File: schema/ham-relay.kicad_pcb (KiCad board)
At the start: 2 copper layers, 62 parts, among them P1 CONN_01X08, P2 RESET, P3 ISP, P4 CONN_01X03, P5 JTAG, U1 CPC1017N, U2 XYZ, U3 REG 3V3, U4 XYZ, U5 TBB1458, U6 LPC1114FN28/102

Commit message: Update schematics
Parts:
- added TP1: TESTPOINT, Measurement_Points:Measurement_Point_Round-SMD-Pad_Small, F.Cu at (189.2, 41.9)
- added TP10: TESTPOINT, Measurement_Points:Measurement_Point_Round-SMD-Pad_Small, F.Cu at (228.6, 20.3)
- added TP2: TESTPOINT, Measurement_Points:Measurement_Point_Round-SMD-Pad_Small, F.Cu at (264.2, 113.0)
- added TP3: TESTPOINT, Measurement_Points:Measurement_Point_Round-SMD-Pad_Small, F.Cu at (251.5, 139.7)
- added TP4: TESTPOINT, Measurement_Points:Measurement_Point_Round-SMD-Pad_Small, F.Cu at (195.6, 152.4)
- added TP5: TESTPOINT, Measurement_Points:Measurement_Point_Round-SMD-Pad_Small, F.Cu at (226.1, 113.0)
- added TP6: TESTPOINT, Measurement_Points:Measurement_Point_Round-SMD-Pad_Small, F.Cu at (264.2, 73.7)
- added TP7: TESTPOINT, Measurement_Points:Measurement_Point_Round-SMD-Pad_Small, F.Cu at (195.6, 138.4)
- added TP8: TESTPOINT, Measurement_Points:Measurement_Point_Round-SMD-Pad_Small, F.Cu at (189.2, 34.3)
- added TP9: TESTPOINT, Measurement_Points:Measurement_Point_Round-SMD-Pad_Small, F.Cu at (217.2, 20.3)
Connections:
- C15 pad 2: /MOD_OUT -> /AUDIO_OUT
- P3 pad 1: GND -> Net-(P3-Pad1)
- P3 pad 2: Net-(P3-Pad2) -> GND
- R21 pad 1: /MOD_OUT -> /AUDIO_OUT
- R22 pad 2: Net-(P3-Pad2) -> Net-(P3-Pad1)
- U3 pad 1: VCC -> (no net)
- U3 pad 2: +3V3 -> (no net)
- U3 pad 3: GND -> (no net)
- U6 pad 24: Net-(P3-Pad2) -> Net-(P3-Pad1)
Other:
- board text added: "+12V"
- board text added: "+3V3"
- board text added: "AUDIO_OUT"
- board text added: "GND"
- board text added: "TONE"
- board text added: "TONE_SW"
- board text added: "VCC"
- board text added: "VCC/2"

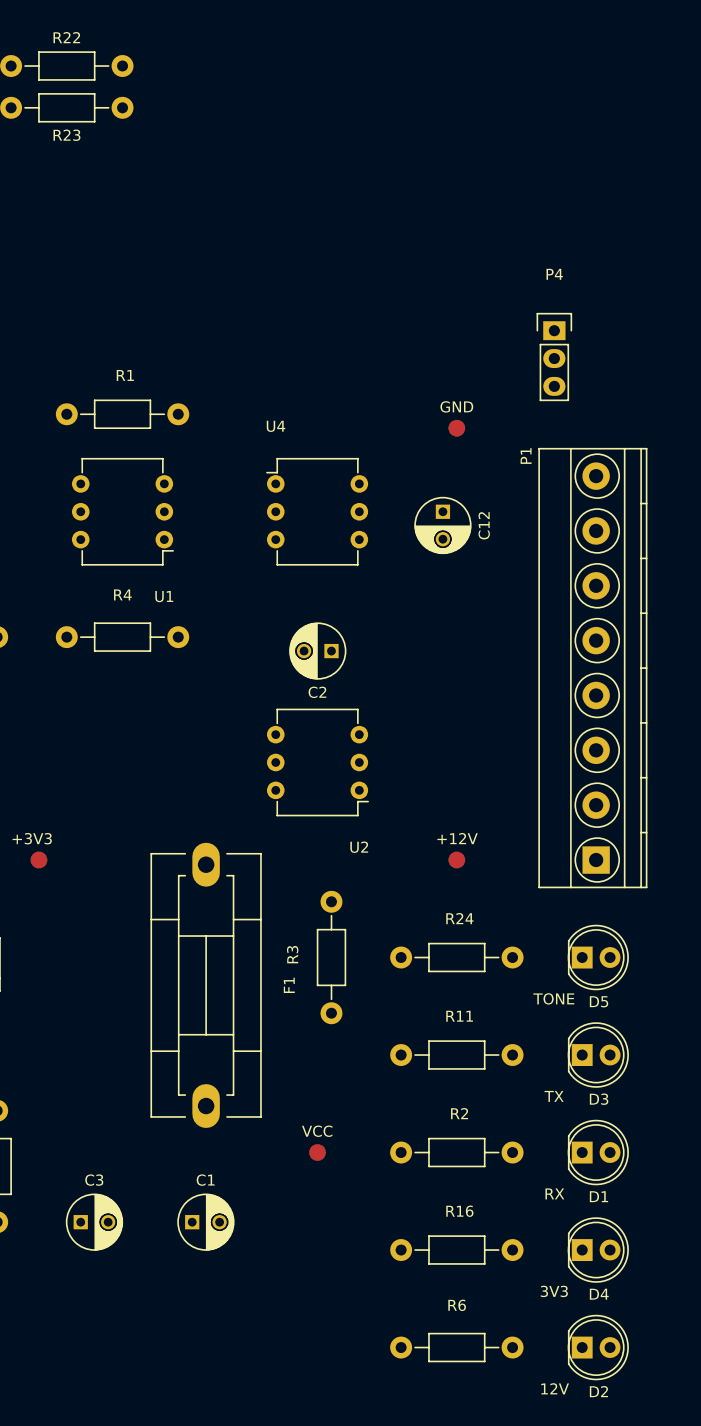
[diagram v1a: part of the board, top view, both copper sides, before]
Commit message: Add status LED on schematics
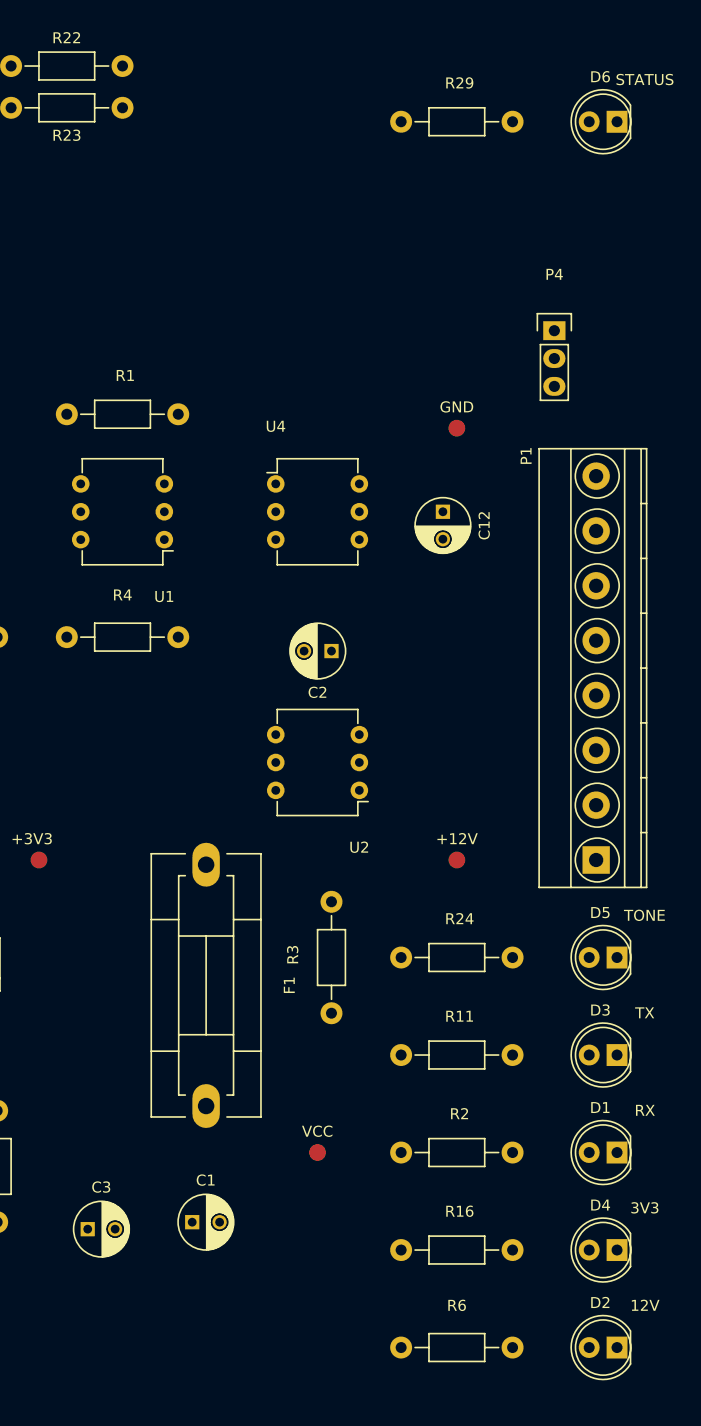
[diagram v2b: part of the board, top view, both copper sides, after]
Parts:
- added D6: STATUS, LEDs:LED-5MM, F.Cu at (278.8, 45.7)
- added R29: 560, Resistors_ThroughHole:Resistor_Horizontal_RM10mm, F.Cu at (264.2, 45.7)
- moved D1 3.18 mm to (278.8, 139.7), turned to 180 degrees
- moved D2 3.18 mm to (278.8, 157.5), turned to 180 degrees
- moved D3 3.18 mm to (278.8, 130.8), turned to 180 degrees
- moved D4 3.18 mm to (278.8, 148.6), turned to 180 degrees
- moved D5 3.18 mm to (278.8, 121.9), turned to 180 degrees
- moved C3 0.90 mm to (230.5, 146.7)
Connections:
- P1 pad 6: Net-(P1-Pad6) -> (no net)
- P1 pad 7: Net-(P1-Pad7) -> (no net)
- P5 pad 15: Net-(P5-Pad15) -> (no net)
- P5 pad 19: Net-(P5-Pad19) -> (no net)
- P5 pad 3: Net-(P5-Pad3) -> (no net)
- P5 pad 5: Net-(P5-Pad5) -> (no net)
- U2 pad 6: Net-(U2-Pad6) -> (no net)
- U4 pad 6: Net-(U4-Pad6) -> (no net)
- U6 pad 1: Net-(U6-Pad1) -> /TONE
- U6 pad 10: Net-(U6-Pad10) -> (no net)
- U6 pad 11: Net-(U6-Pad11) -> (no net)
- U6 pad 13: Net-(U6-Pad13) -> (no net)
- U6 pad 14: Net-(U6-Pad14) -> (no net)
- U6 pad 17: Net-(U6-Pad17) -> (no net)
- U6 pad 18: Net-(U6-Pad18) -> (no net)
- U6 pad 19: Net-(U6-Pad19) -> (no net)
- U6 pad 25: Net-(U6-Pad25) -> (no net)
- U6 pad 26: Net-(U6-Pad26) -> (no net)
- U6 pad 4: /TONE -> (no net)

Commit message: First routing
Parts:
- removed TP1, TP10, TP2, TP3, TP4, TP5, TP6, TP7, TP8, TP9: TESTPOINT, Measurement_Points:Measurement_Point_Round-SMD-Pad_Small
- added IC1: 74HC126N, Housings_DIP:DIP-14_W7.62mm, F.Cu at (136.5, 120.0)
- added J1: DB9, w_conn_d-sub:DB_9F, F.Cu at (62.2, 117.5)
- C10: value 10µF -> 330nF
- C11: value 1µF -> 100nF
- C12: value 10nF -> 47nF
- C13, C14: value 100nF -> 10µF
- C3: value 10nF -> 10µF
- C4: value 330nF -> 1µF
- C5: value 100nF -> 1µF
- C6: value 10µF -> 100nF
- C7: value 47nF -> 100nF
- C8: value 1µF -> 10nF
- C9: value 10µF -> 10nF
- D1: value RX -> 12V
- D2: value 12V -> 3V3
- D3: value TX -> TONE
- D4: value 3V3 -> RX
- D5: value TONE -> TX
- F1: footprint Fuse_Holders_and_Fuses:Fuseholder5x20_horiz_SemiClosed_Casing10x25mm -> Fuse_5x20mm_Holder:Fuse_5x20mm_Holder
- P1: value CONN_01X08 -> JTAG; footprint Terminal_Blocks:TerminalBlock_Pheonix_MKDS1.5-8pol -> Pin_Headers:Pin_Header_Straight_2x10
- P2: value RESET -> CONN_01X08; footprint Pin_Headers:Pin_Header_Straight_1x02 -> Terminal_Blocks:TerminalBlock_Pheonix_MKDS1.5-8pol
- P3: value ISP -> RESET
- P4: value CONN_01X03 -> ISP; footprint Pin_Headers:Pin_Header_Straight_1x03 -> Pin_Headers:Pin_Header_Straight_1x02
- P5: value JTAG -> CONN_01X03; footprint Pin_Headers:Pin_Header_Straight_2x10 -> Pin_Headers:Pin_Header_Straight_1x03
- R1, R2, R3: value ? -> 10k
- R10: value 5k6 -> ?
- R11: value 560 -> 2k2
- R12: value 1k8 -> 10k
- R13: value 560 -> 10k
- R14, R15, R8: value 47k -> ?
- R16: value ? -> 560
- R17, R18: value 220k -> 560
- R19: value 1k2 -> 680
- R20: value 1k2 -> 1k8
- R21: value 1k8 -> 5k6
- R22: value 10k -> 1k8
- R23: value 10k -> 47k
- R24: value 560 -> 47k
- R25, R26: value 10k -> 220k
- R27, R28: value 10k -> 1k2
- R29: value 560 -> 1k8
- R4: value 2k2 -> 10k
- R5: value 680 -> ?
- R6: value ? -> 47k
- R7: value 1k8 -> 47k
- R9: value 47k -> 560
- RV1, RV2: footprint Potentiometers:Potentiometer_Bourns_3005_Angular_ScrewFront -> Potentiometers:Potentiometer_Triwood_RM-065
- U1: value CPC1017N -> REG 3V3; footprint Housings_DIP:DIP-6_W7.62mm -> TO_SOT_Packages_THT:TO-220_Neutral123_Horizontal
- U2: value XYZ -> LPC1114FN28/102; footprint Housings_DIP:DIP-6_W7.62mm -> Housings_DIP:DIP-28_W15.24mm
- U3: value REG 3V3 -> CPC1017N; footprint TO_SOT_Packages_THT:TO-220_Neutral123_Vertical -> Housings_DIP:DIP-6_W7.62mm
- U5: value TBB1458 -> XYZ; footprint Housings_DIP:DIP-8_W7.62mm -> Housings_DIP:DIP-6_W7.62mm
- U6: value LPC1114FN28/102 -> TBB1458; footprint Housings_DIP:DIP-28_W15.24mm -> Housings_DIP:DIP-8_W7.62mm
- moved D4 242.8 mm to (60.3, 42.5), turned to 0 degrees
- moved D3 229.9 mm to (60.3, 59.1), turned to 0 degrees
- moved D5 229.7 mm to (60.3, 50.8), turned to 0 degrees
- moved D6 219.1 mm to (60.7, 67.3), turned to 0 degrees
- moved R16 215.3 mm to (72.4, 50.8), turned to 180 degrees
- moved P1 196.2 mm to (81.3, 128.9), turned to 180 degrees
- moved R3 173.8 mm to (80.0, 102.2), turned to 180 degrees
- moved R2 169.6 mm to (99.1, 101.0), turned to 270 degrees
- moved R1 165.1 mm to (80.0, 132.7)
- moved R9 163.0 mm to (72.4, 59.1), turned to 180 degrees
- moved R13 162.4 mm to (87.6, 112.4), turned to 90 degrees
- moved P4 162.3 mm to (125.1, 131.4), turned to 90 degrees
- moved R4 153.8 mm to (80.0, 98.4), turned to 180 degrees
- moved P3 145.5 mm to (114.3, 131.4), turned to 90 degrees
- moved R6 141.1 mm to (173.4, 49.5), turned to 180 degrees
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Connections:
- C10 pad 2: Net-(C10-Pad2) -> GND
- C11 pad 1: +3V3 -> Net-(C11-Pad1)
- C12 pad 1: /TX_CR -> Net-(C12-Pad1)
- C13 pad 1: +3V3 -> Net-(C13-Pad1)
- C13 pad 2: GND -> Net-(C13-Pad2)
- C14 pad 1: +3V3 -> Net-(C14-Pad1)
- C14 pad 2: GND -> Net-(C14-Pad2)
- C15 pad 2: /AUDIO_OUT -> /Audio/AUDIO_OUT
- C2 pad 1: /RX_CR -> VCC
- C3 pad 1: VCC -> VCC/2
- C4 pad 1: Net-(C4-Pad1) -> VCC
- C5 pad 1: Net-(C5-Pad1) -> +3V3
- C6 pad 1: VCC/2 -> +3V3
- C7 pad 1: Net-(C7-Pad1) -> +3V3
- C8 pad 1: VCC -> /RX_CR
- C9 pad 1: Net-(C9-Pad1) -> /TX_CR
- C9 pad 2: Net-(C9-Pad2) -> GND
- D1 pad 1: /RX_CR -> GND
- D4 pad 1: GND -> /RX_CR
- P1 pad 1: +12V -> +3V3
- P1 pad 2: /AUDIO_IN -> +3V3
- P1 pad 3: /AUDIO_OUT -> (no net)
- P1 pad 4: /RX_CR -> GND
- P1 pad 5: /TX_CR -> (no net)
- P1 pad 6: (no net) -> GND
- P1 pad 7: (no net) -> /SWDIO
- P2 pad 1: Net-(P2-Pad1) -> +12V
- P2 pad 2: GND -> /Audio/AUDIO_IN
- P3 pad 1: Net-(P3-Pad1) -> /RESET
- P4 pad 1: /RX -> /ISP
- P4 pad 2: /TX -> GND
- P5 pad 1: +3V3 -> /RX
- P5 pad 2: +3V3 -> /TX
- P5 pad 3: (no net) -> GND
- R1 pad 1: /TONE_SW -> /SWCLK
- R1 pad 2: Net-(R1-Pad2) -> GND
- R10 pad 1: Net-(C7-Pad1) -> /TONE_SW
- R10 pad 2: Net-(C5-Pad1) -> Net-(R10-Pad2)
- R11 pad 1: /TXE -> /Audio/TONE
- R11 pad 2: Net-(D3-Pad2) -> GND
- R12 pad 1: /AUDIO_IN -> +3V3
- R12 pad 2: GND -> /RESET
- R13 pad 1: /TXE -> +3V3
- R13 pad 2: Net-(R13-Pad2) -> /ISP
- R14 pad 1: Net-(C9-Pad1) -> VCC
- R14 pad 2: Net-(R14-Pad2) -> Net-(D4-Pad2)
- R15 pad 1: Net-(C10-Pad1) -> VCC
- R16 pad 1: +3V3 -> /TXE
- R16 pad 2: Net-(D4-Pad2) -> Net-(D5-Pad2)
- R17 pad 1: Net-(R14-Pad2) -> Net-(IC1-Pad8)
- R17 pad 2: Net-(R17-Pad2) -> Net-(D6-Pad2)
- R18 pad 1: Net-(R15-Pad2) -> /TXE
- R19 pad 1: Net-(R17-Pad2) -> Net-(C10-Pad1)
- R19 pad 2: Net-(C15-Pad1) -> /Audio/TONE
- R2 pad 1: VCC -> +3V3
- R2 pad 2: Net-(D1-Pad2) -> /SWDIO
- R20 pad 1: Net-(R18-Pad2) -> Net-(C11-Pad1)
- R20 pad 2: Net-(C15-Pad1) -> Net-(C10-Pad1)
- R21 pad 1: /AUDIO_OUT -> Net-(C12-Pad1)
- R21 pad 2: GND -> Net-(C11-Pad1)
- R22 pad 1: +3V3 -> /Audio/AUDIO_IN
- R22 pad 2: Net-(P3-Pad1) -> GND
- R23 pad 1: +3V3 -> Net-(C13-Pad1)
- R23 pad 2: Net-(P2-Pad1) -> Net-(R23-Pad2)
- R24 pad 1: Net-(R24-Pad1) -> Net-(C14-Pad1)
- R24 pad 2: Net-(D5-Pad2) -> Net-(R24-Pad2)
- R25 pad 1: +3V3 -> Net-(R23-Pad2)
- R25 pad 2: Net-(P5-Pad7) -> Net-(R25-Pad2)
- R26 pad 1: Net-(P5-Pad9) -> Net-(R24-Pad2)
- R26 pad 2: GND -> Net-(R26-Pad2)
- R27 pad 1: Net-(P5-Pad11) -> Net-(R25-Pad2)
- R27 pad 2: GND -> Net-(C15-Pad1)
- R28 pad 1: Net-(P5-Pad17) -> Net-(R26-Pad2)
- R28 pad 2: GND -> Net-(C15-Pad1)
- R29 pad 1: Net-(R29-Pad1) -> /Audio/AUDIO_OUT
- R29 pad 2: Net-(D6-Pad2) -> GND
- R3 pad 1: VCC -> Net-(P1-Pad11)
- R3 pad 2: Net-(R3-Pad2) -> GND
- R4 pad 1: Net-(R4-Pad1) -> Net-(P1-Pad17)
- R5 pad 1: Net-(C4-Pad1) -> VCC
- R5 pad 2: Net-(R4-Pad1) -> Net-(D1-Pad2)
- R6 pad 2: Net-(D2-Pad2) -> VCC/2
- R7 pad 1: Net-(C5-Pad1) -> VCC/2
- R7 pad 2: Net-(C4-Pad1) -> GND
- R8 pad 1: VCC -> +3V3
- R8 pad 2: VCC/2 -> Net-(D2-Pad2)
- R9 pad 1: VCC/2 -> /TONE_SW
- R9 pad 2: GND -> Net-(D3-Pad2)
- RV1 pad 1: Net-(C7-Pad1) -> Net-(C12-Pad1)
- RV1 pad 2: Net-(C9-Pad2) -> Net-(C13-Pad2)
- RV2 pad 1: /AUDIO_IN -> /Audio/AUDIO_IN
- RV2 pad 2: Net-(C10-Pad2) -> Net-(C14-Pad2)
- U1 pad 1: Net-(R1-Pad2) -> GND
- U1 pad 2: GND -> +3V3
- U1 pad 3: Net-(R4-Pad1) -> VCC
- U2 pad 1: Net-(R3-Pad2) -> /TONE
- U2 pad 2: /RX_CR -> /SWO
- U2 pad 3: (no net) -> /SWCLK
- U2 pad 4: GND -> (no net)
- U2 pad 5: /RXE -> Net-(IC1-Pad2)
- U4 pad 1: Net-(R13-Pad2) -> Net-(R15-Pad2)
- U4 pad 2: GND -> /RX_CR
- U4 pad 5: /TX_CR -> /RXE
- U5 pad 1: Net-(R17-Pad2) -> Net-(R18-Pad2)
- U5 pad 2: Net-(R14-Pad2) -> GND
- U5 pad 3: VCC/2 -> (no net)
- U5 pad 5: VCC/2 -> /TX_CR
- U5 pad 6: Net-(R15-Pad2) -> (no net)
- U6 pad 1: /TONE -> Net-(R25-Pad2)
- U6 pad 2: Net-(P5-Pad13) -> Net-(R23-Pad2)
- U6 pad 3: Net-(P5-Pad9) -> VCC/2
- U6 pad 4: (no net) -> GND
- U6 pad 5: /TONE_SW -> VCC/2
- U6 pad 6: Net-(R24-Pad1) -> Net-(R24-Pad2)
- U6 pad 7: +3V3 -> Net-(R26-Pad2)
- U6 pad 8: GND -> VCC
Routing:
- net VCC: track 0.00 -> 288.2 mm
- net /RX_CR: track 0.00 -> 261.1 mm
- net +3V3: track 0.00 -> 234.5 mm
- net /TONE_SW: track 0.00 -> 155.4 mm, vias 0 -> 1
- net /TXE: track 0.00 -> 143.9 mm, vias 0 -> 1
- net /ISP: track 0.00 -> 121.5 mm
- net Net-(IC1-Pad8): track 0.00 -> 106.0 mm
- net /RESET: track 0.00 -> 88.0 mm
- net Net-(C15-Pad1): track 0.00 -> 84.8 mm
- net /SWCLK: track 0.00 -> 83.5 mm, vias 0 -> 1
- net VCC/2: track 0.00 -> 74.1 mm
- net /Audio/AUDIO_IN: track 0.00 -> 72.7 mm
- net /TX_CR: track 0.00 -> 61.1 mm
- net /SWO: track 0.00 -> 58.6 mm
- net +12V: track 0.00 -> 48.6 mm
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- added copper zone on B.Cu, net GND
- added copper zone on F.Cu, net GND
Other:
- board outline added: 140 x 98 mm
- board text removed: "+12V"
- board text removed: "+3V3"
- board text removed: "AUDIO_OUT"
- board text removed: "GND"
- board text removed: "TONE"
- board text removed: "TONE_SW"
- board text removed: "VCC"
- board text removed: "VCC/2"

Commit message: More changes
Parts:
- removed C4: 1µF, Capacitors_ThroughHole:C_Radial_D5_L6_P2.5
- removed IC1: 74HC126N, Housings_DIP:DIP-14_W7.62mm
- added R30: 22k, resistors:Resistor_Horizontal_RM08mm, F.Cu at (127.8, 146.2)
- added U7: 74HC126N, Housings_DIP:DIP-14_W7.62mm, F.Cu at (156.8, 95.9)
- C1, C13, C14, C15, C3, C5: footprint Capacitors_ThroughHole:C_Radial_D5_L6_P2.5 -> Capacitors_ThroughHole:C_Radial_D5_L11_P2.5
- C10, C11: footprint Capacitors_ThroughHole:C_Radial_D5_L6_P2.5 -> Capacitors_ThroughHole:C_Rect_L7_W3.5_P5
- C12: value 47nF -> 33nF; footprint Capacitors_ThroughHole:C_Radial_D5_L6_P2.5 -> Capacitors_ThroughHole:C_Rect_L7_W3.5_P5
- C2, C6, C7, C8, C9: footprint Capacitors_ThroughHole:C_Radial_D5_L6_P2.5 -> Capacitors_ThroughHole:C_Rect_L4_W2.5_P2.5
- D1, D2, D3, D4, D5, D6: footprint LEDs:LED-5MM -> LEDs:LED-3MM
- F1: footprint Fuse_5x20mm_Holder:Fuse_5x20mm_Holder -> Fuse_Holders_and_Fuses:Fuseholder5x20_horiz_open_lateral_Type-II
- R1, R10, R11, R12, R13, R14, R15, R16, R17, R18, R2, R20, R21, R22, R23, R24, R25, R26, R27, R28, R29, R3, R4, R5, R6, R7, R8, R9: footprint Resistors_ThroughHole:Resistor_Horizontal_RM10mm -> resistors:Resistor_Horizontal_RM08mm
- R19: value 680 -> 560; footprint Resistors_ThroughHole:Resistor_Horizontal_RM10mm -> resistors:Resistor_Horizontal_RM08mm
- RV1: value 22k -> 10k; footprint Potentiometers:Potentiometer_Triwood_RM-065 -> Potentiometres:POT93YB
- RV2: footprint Potentiometers:Potentiometer_Triwood_RM-065 -> Potentiometres:POT93YA
- U1: value REG 3V3 -> REG3V3
- moved R2 105.5 mm to (24.8, 26.0)
- moved C12 99.5 mm to (50.2, 22.2)
- moved R21 99.5 mm to (45.1, 18.4)
- moved C10 99.5 mm to (36.2, 28.6)
- moved R11 99.5 mm to (55.2, 28.6)
- moved R19 99.5 mm to (45.1, 28.6)
- moved R20 99.5 mm to (40.0, 23.5)
- moved R22 99.5 mm to (60.3, 23.5)
- moved R29 74.2 mm to (162.6, 160.7)
- moved C15 70.6 mm to (170.2, 156.2)
- moved U6 65.6 mm to (104.1, 3.17)
- moved C11 65.6 mm to (87.6, 22.2)
- moved C13 65.6 mm to (96.5, 2.54)
- moved C14 65.6 mm to (118.1, 2.54)
- moved R23 65.6 mm to (90.8, 4.45)
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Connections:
- P2 pad 1: +12V -> GND
- P2 pad 2: /Audio/AUDIO_IN -> /RX_CR
- P2 pad 3: /Audio/AUDIO_OUT -> /TX_CR
- P2 pad 4: /RX_CR -> /Audio/AUDIO_IN
- P2 pad 5: /TX_CR -> /Audio/AUDIO_OUT
- P2 pad 8: GND -> +12V
- RV1 pad 1: Net-(C12-Pad1) -> Net-(R30-Pad1)
- U1 pad 1: GND -> VCC
- U1 pad 2: +3V3 -> GND
- U1 pad 3: VCC -> +3V3
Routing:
- net /RX_CR: track 261.1 -> 19.7 mm
- net +3V3: track 234.5 -> 2.54 mm
- net /TONE_SW: track 155.4 -> 8.26 mm, vias 1 -> 0
- net /TXE: track 143.9 -> 0.00 mm, vias 1 -> 0
- net /ISP: track 121.5 -> 0.00 mm
- net VCC: track 288.2 -> 179.4 mm
- net Net-(R17-Pad1): track 106.0 -> 0.00 mm
- net /RESET: track 88.0 -> 0.00 mm
- net Net-(C15-Pad1): track 84.8 -> 0.00 mm
- net /SWCLK: track 83.5 -> 0.00 mm, vias 1 -> 0
- net /Audio/AUDIO_IN: track 72.7 -> 0.00 mm
- net VCC/2: track 74.1 -> 6.98 mm
- net /SWO: track 58.6 -> 0.00 mm
- net Net-(U2-Pad9): track 48.5 -> 0.00 mm, vias 1 -> 0
- net /TX_CR: track 61.1 -> 13.4 mm
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- added copper zone on B.Cu, net +12V
- added copper zone on B.Cu, net VCC
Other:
- outline, holes or cut-outs redrawn
- net class Default: clearance 0.2 -> 0.5; trace_width 0.25 -> 1; via_dia 0.6 -> 2.5; via_drill 0.4 -> 1
- net class Small added: clearance 508, trace_width 254, via_dia 2.5, via_drill 1
- rule trace_clearance: 0.2 -> 0.5

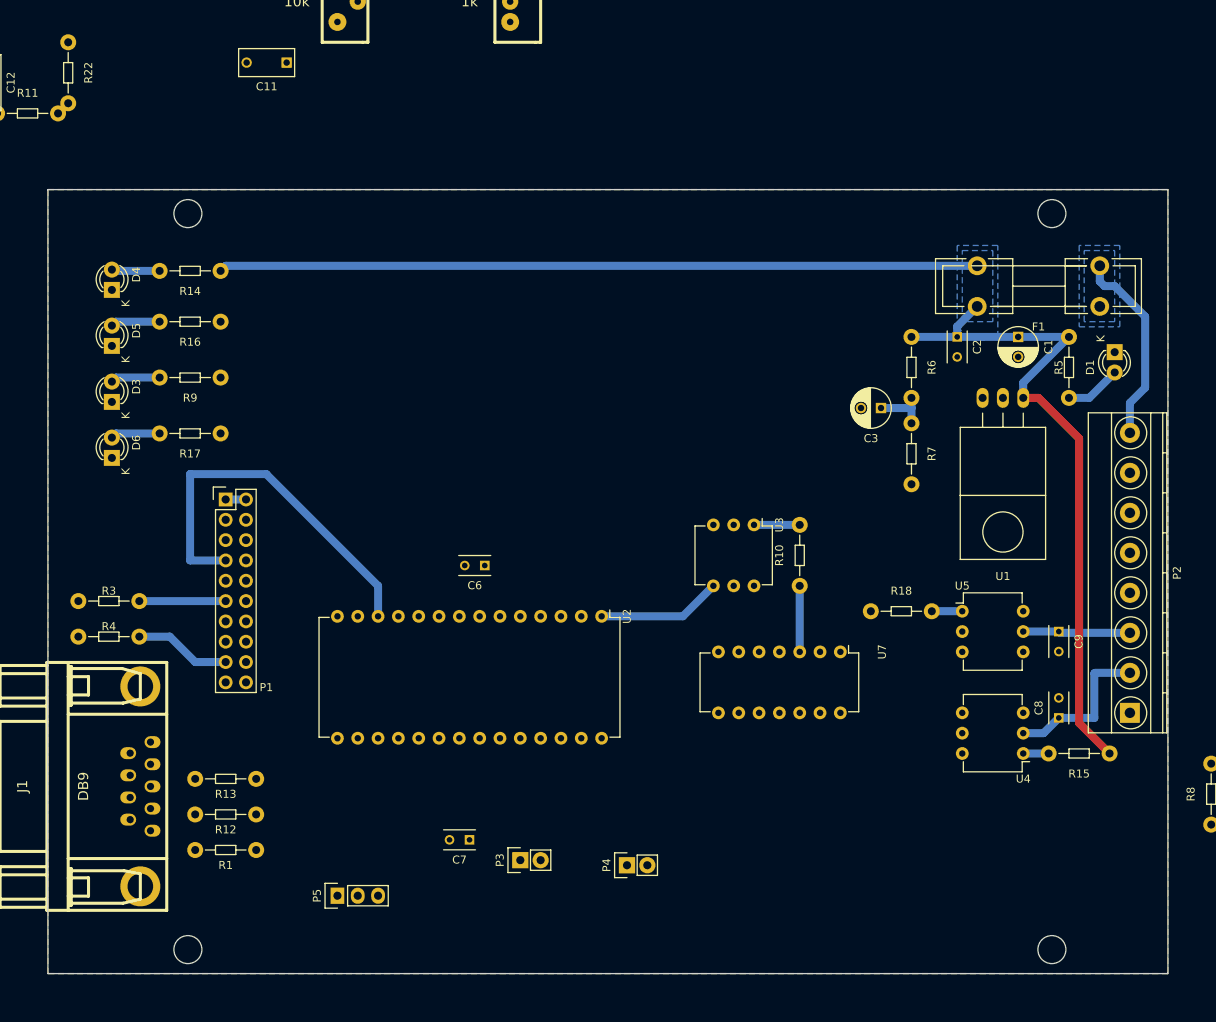
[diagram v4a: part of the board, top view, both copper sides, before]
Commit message: Update footprints
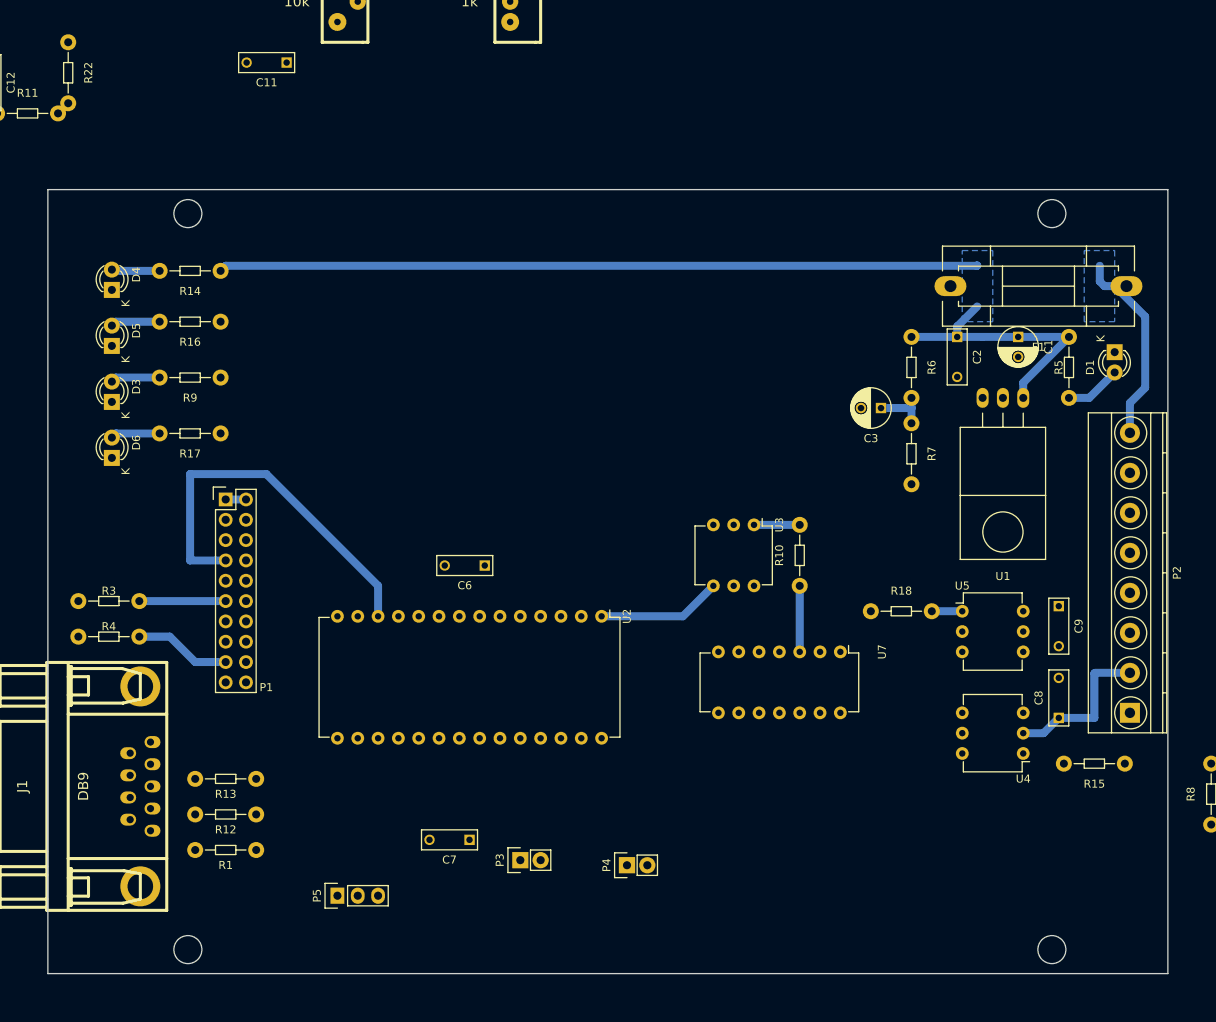
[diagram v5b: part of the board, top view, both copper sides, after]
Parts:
- C11: footprint Capacitors_ThroughHole:C_Rect_L7_W3.5_P5 -> Capacitors_ThroughHole:C_Rect_L7_W2.5_P5
- C2, C6, C7, C8, C9: footprint Capacitors_ThroughHole:C_Rect_L4_W2.5_P2.5 -> Capacitors_ThroughHole:C_Rect_L7_W2.5_P5
- F1: footprint Fuse_Holders_and_Fuses:Fuseholder5x20_horiz_open_lateral_Type-II -> Fuse_Holders_and_Fuses:Fuseholder5x20_horiz_SemiClosed_Casing10x25mm
- moved C9 3.17 mm to (184.2, 90.2)
- moved R15 2.29 mm to (188.6, 109.9)
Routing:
- net VCC: track 179.4 -> 129.4 mm
- net /TX_CR: track 13.4 -> 0.00 mm
- net Net-(R15-Pad2): track 3.17 -> 0.00 mm
- removed copper zone on B.Cu, net GND
- removed copper zone on F.Cu, net GND
